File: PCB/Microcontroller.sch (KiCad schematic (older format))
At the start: 19 parts, among them U8 ATSAM4S, Y1 12MHz .25%

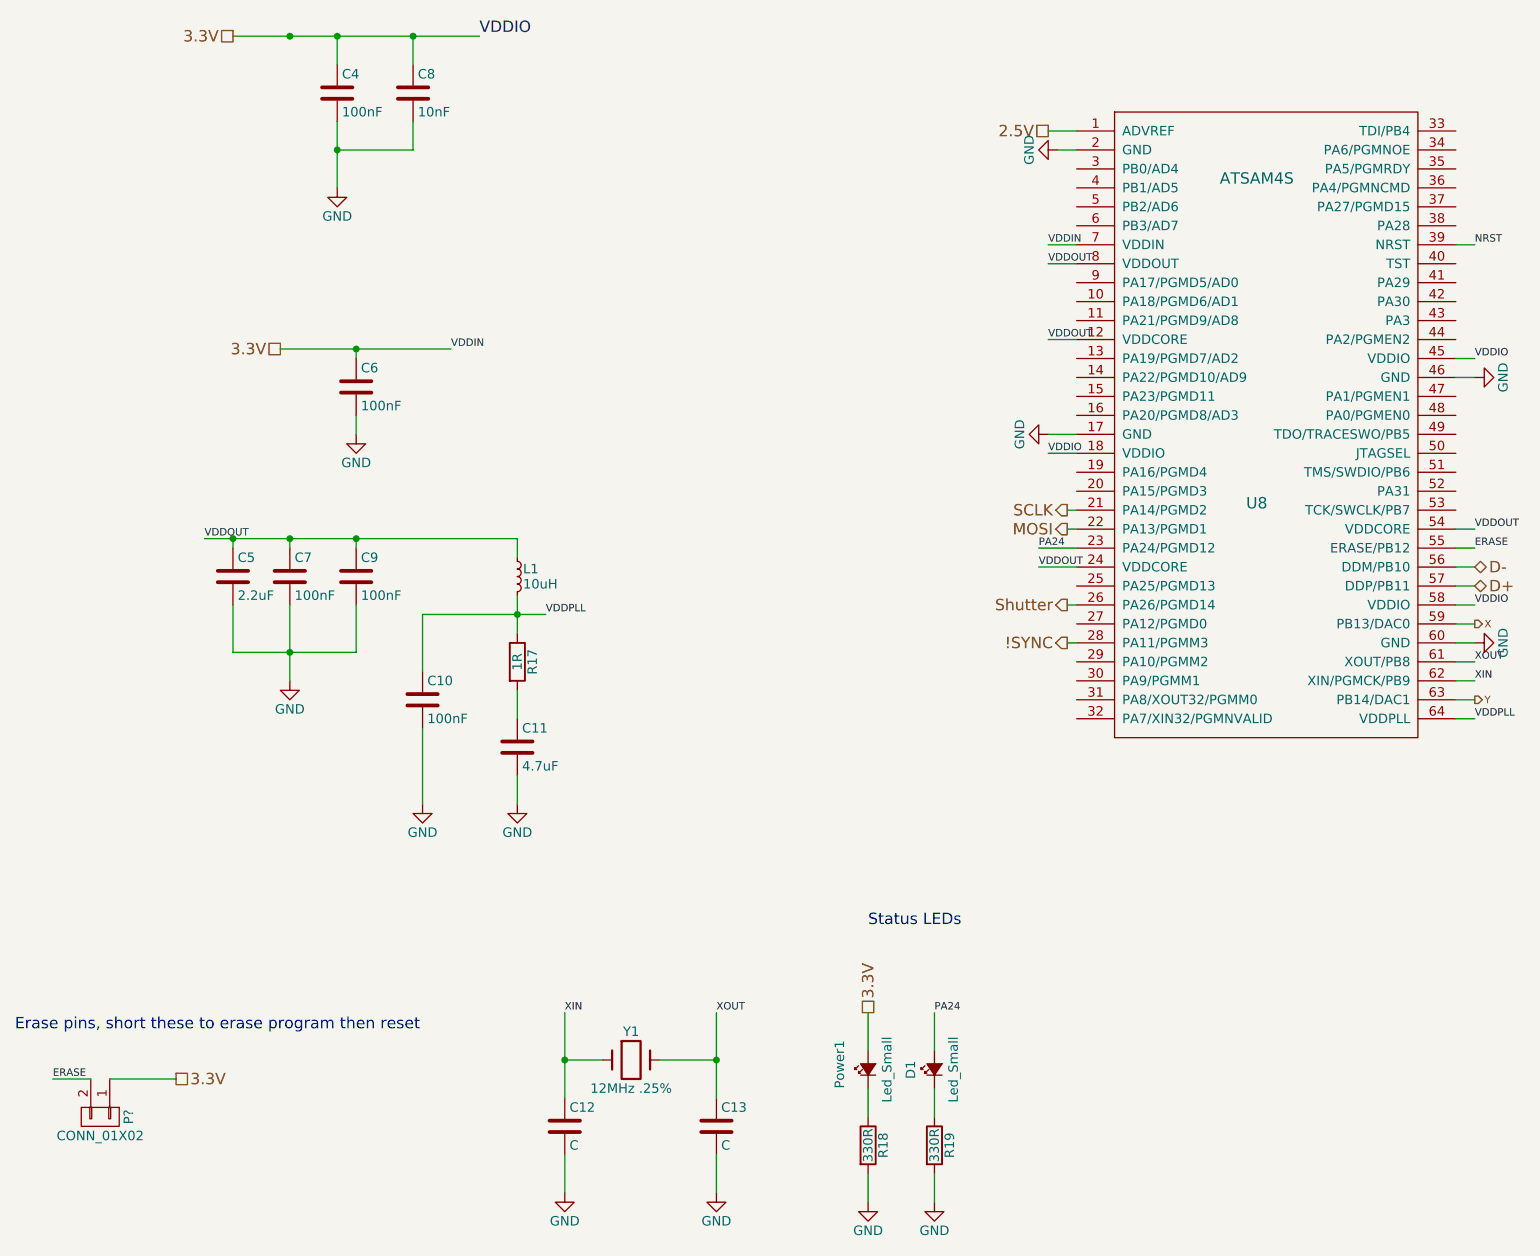
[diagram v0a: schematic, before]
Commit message: Reannotated Components
Annotated components to standards,
TODO: Add Silkscreen for signals on bottom
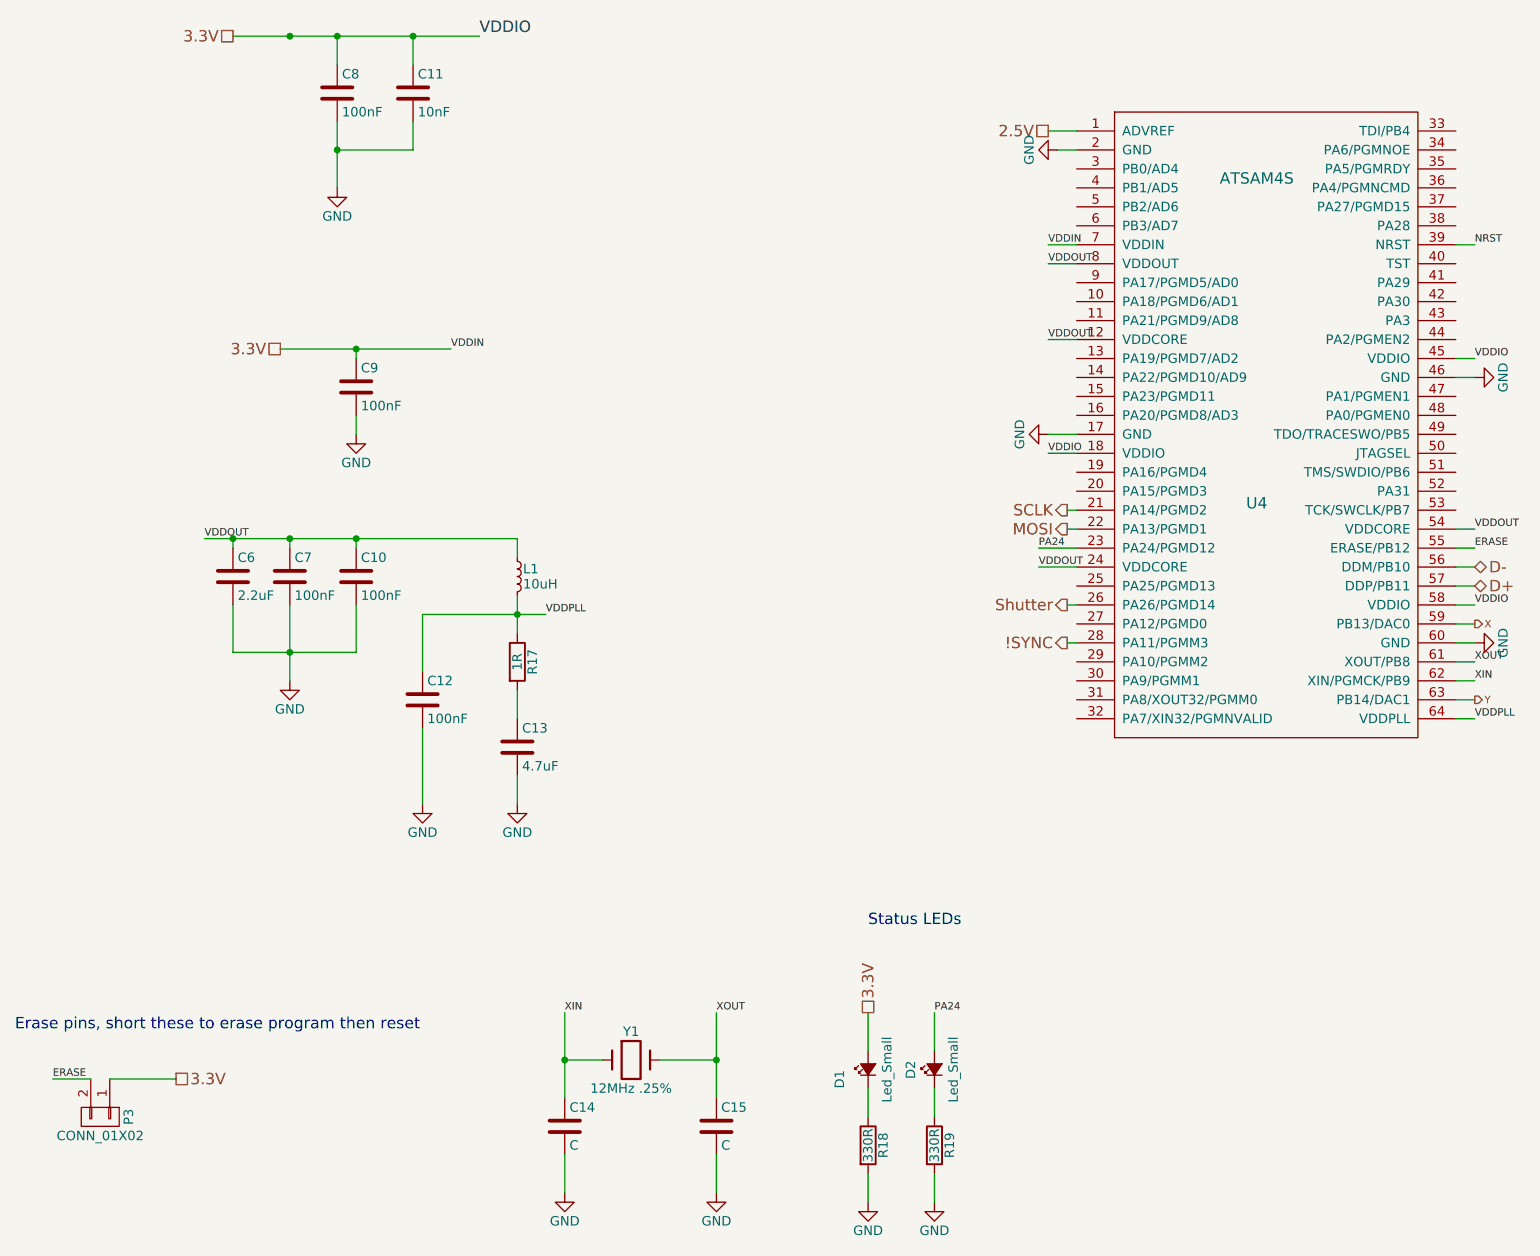
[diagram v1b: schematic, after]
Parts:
- gave numbers to parts that had none: 1
- renumbered C9 to C10, C8 to C11, C10 to C12, C11 to C13, C12 to C14, C13 to C15, C5 to C6, C4 to C8, C6 to C9, Power1 to D1, D1 to D2, U8 to U4
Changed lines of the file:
@@
 $EndDescr
 $Comp
-L ATSAM4S U8
+L ATSAM4S U4
 U 1 1 56B20B8A
 P 7250 2450
-F 0 "U8" H 7250 1137 60  0000 C CNN
+F 0 "U4" H 7250 1137 60  0000 C CNN
 F 1 "ATSAM4S" H 7250 2850 60  0000 C CNN
 F 2 "Housings_QFP:LQFP-64_10x10mm_Pitch0.5mm" H 7250 2850 60  0001 C CNN
@@
 3.3V
 $Comp
-L C C4
+L C C8
 U 1 1 56B26047
 P 2400 1600
-F 0 "C4" H 2425 1700 50  0000 L CNN
+F 0 "C8" H 2425 1700 50  0000 L CNN
 F 1 "100nF" H 2425 1500 50  0000 L CNN
 F 2 "Capacitors_SMD:C_0402" H 2438 1450 50  0001 C CNN
@@
 $EndComp
 $Comp
-L C C8
+L C C11
 U 1 1 56B26074
 P 2800 1600
-F 0 "C8" H 2825 1700 50  0000 L CNN
+F 0 "C11" H 2825 1700 50  0000 L CNN
 F 1 "10nF" H 2825 1500 50  0000 L CNN
 F 2 "Capacitors_SMD:C_0402" H 2838 1450 50  0001 C CNN
@@
 $EndComp
 $Comp
-L C C6
+L C C9
 U 1 1 56B26180
 P 2500 3150
-F 0 "C6" H 2525 3250 50  0000 L CNN
+F 0 "C9" H 2525 3250 50  0000 L CNN
 F 1 "100nF" H 2525 3050 50  0000 L CNN
 F 2 "Capacitors_SMD:C_0402" H 2538 3000 50  0001 C CNN
@@
 $EndComp
 $Comp
-L C C9
+L C C10
 U 1 1 56B262EF
 P 2500 4150
-F 0 "C9" H 2525 4250 50  0000 L CNN
+F 0 "C10" H 2525 4250 50  0000 L CNN
 F 1 "100nF" H 2525 4050 50  0000 L CNN
 F 2 "Capacitors_SMD:C_0402" H 2538 4000 50  0001 C CNN
@@
 $EndComp
 $Comp
-L C C5
+L C C6
 U 1 1 56B263C7
 P 1850 4150
-F 0 "C5" H 1875 4250 50  0000 L CNN
+F 0 "C6" H 1875 4250 50  0000 L CNN
 F 1 "2.2uF" H 1875 4050 50  0000 L CNN
 F 2 "Capacitors_SMD:C_0603" H 1888 4000 50  0001 C CNN
@@
 $EndComp
 $Comp
-L C C10
+L C C12
 U 1 1 56B26699
 P 2850 4800
-F 0 "C10" H 2875 4900 50  0000 L CNN
+F 0 "C12" H 2875 4900 50  0000 L CNN
 F 1 "100nF" H 2875 4700 50  0000 L CNN
 F 2 "Capacitors_SMD:C_0402" H 2888 4650 50  0001 C CNN
@@
 $EndComp
 $Comp
-L C C11
+L C C13
 U 1 1 56B26716
 P 3350 5050
-F 0 "C11" H 3375 5150 50  0000 L CNN
+F 0 "C13" H 3375 5150 50  0000 L CNN
 F 1 "4.7uF" H 3375 4950 50  0000 L CNN
 F 2 "Capacitors_SMD:C_0603" H 3388 4900 50  0001 C CNN
@@
 $EndComp
 $Comp
-L C C12
+L C C14
 U 1 1 56B28036
 P 3600 7050
-F 0 "C12" H 3625 7150 50  0000 L CNN
+F 0 "C14" H 3625 7150 50  0000 L CNN
 F 1 "C" H 3625 6950 50  0000 L CNN
 F 2 "Capacitors_SMD:C_0402" H 3638 6900 50  0001 C CNN
@@
 $EndComp
 $Comp
-L C C13
+L C C15
 U 1 1 56B2808A
 P 4400 7050
-F 0 "C13" H 4425 7150 50  0000 L CNN
+F 0 "C15" H 4425 7150 50  0000 L CNN
 F 1 "C" H 4425 6950 50  0000 L CNN
 F 2 "Capacitors_SMD:C_0402" H 4438 6900 50  0001 C CNN
@@
 	1550 6800 1200 6800
 $Comp
-L Led_Small Power1
+L Led_Small D1
 U 1 1 56BC8AF6
 P 5200 6750
-F 0 "Power1" H 5100 6900 50  0000 L CNN
+F 0 "D1" H 5100 6900 50  0000 L CNN
 F 1 "Led_Small" H 5025 6650 50  0000 L CNN
 F 2 "LEDs:LED_0603" V 5200 6750 50  0001 C CNN
@@
 $EndComp
 $Comp
-L Led_Small D1
+L Led_Small D2
 U 1 1 56BC8E49
 P 5550 6750
-F 0 "D1" H 5500 6875 50  0000 L CNN
+F 0 "D2" H 5500 6875 50  0000 L CNN
 F 1 "Led_Small" H 5375 6650 50  0000 L CNN
 F 2 "LEDs:LED_0603" V 5550 6750 50  0001 C CNN
@@
 Erase pins, short these to erase program then reset
 $Comp
-L CONN_01X02 P?
+L CONN_01X02 P3
 U 1 1 570CE395
 P 1150 7000
-F 0 "P?" H 1150 7150 50  0000 C CNN
+F 0 "P3" H 1150 7150 50  0000 C CNN
 F 1 "CONN_01X02" V 1250 7000 50  0000 C CNN
 F 2 "" H 1150 7000 50  0000 C CNN

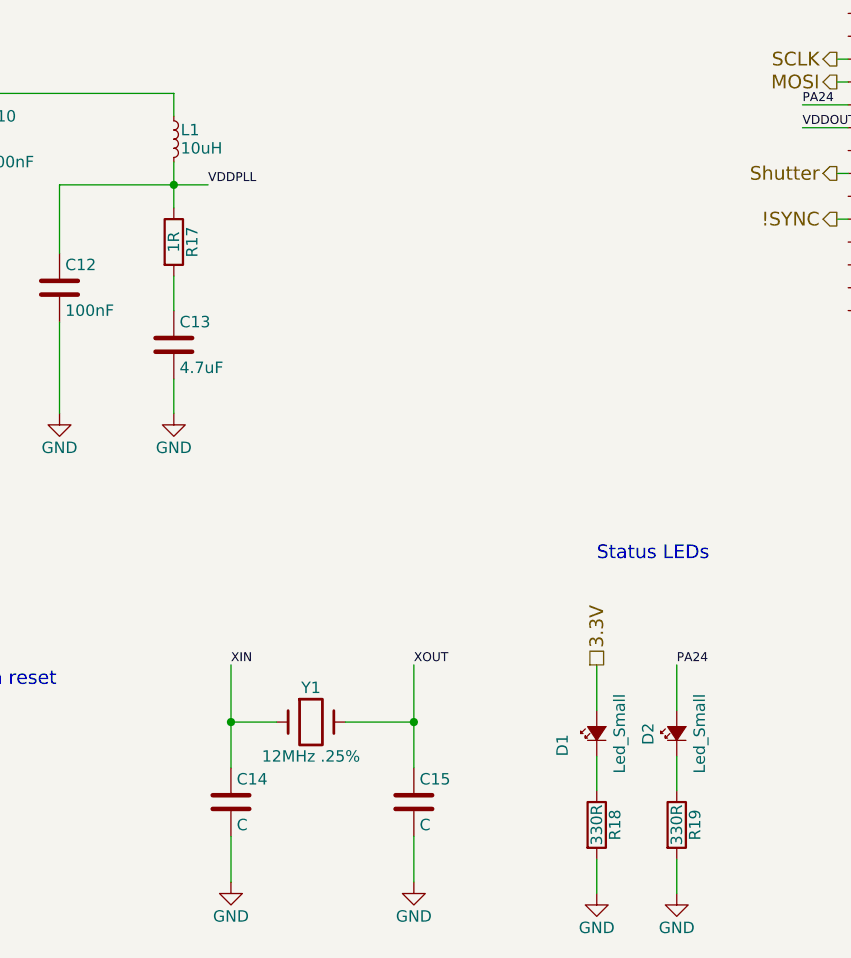
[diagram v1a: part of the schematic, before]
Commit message: Replaced L1 footprint, changed Resistor values
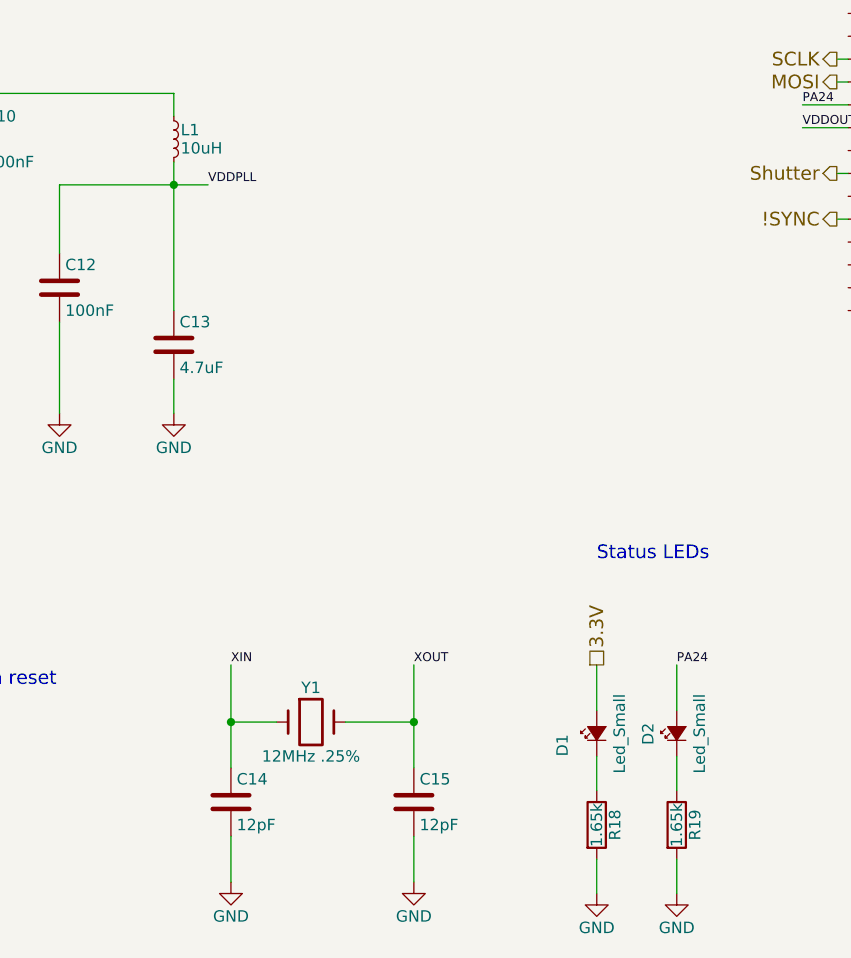
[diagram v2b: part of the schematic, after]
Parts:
- removed R17: 1R, Resistors_SMD:R_0805, symbol R
- C14, C15: value C -> 12pF
- R18, R19: value 330R -> 1.65k
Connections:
- net VDDPLL: now also C13.1
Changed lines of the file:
@@
-$EndComp
-$Comp
-L R R17
-U 1 1 56B26888
-P 3350 4600
-F 0 "R17" V 3430 4600 50  0000 C CNN
-F 1 "1R" V 3350 4600 50  0000 C CNN
-F 2 "Resistors_SMD:R_0805" V 3280 4600 50  0001 C CNN
-F 3 "" H 3350 4600 50  0000 C CNN
-	1    3350 4600
-	1    0    0    -1
 $EndComp
 $Comp
@@
 P 3600 7050
 F 0 "C14" H 3625 7150 50  0000 L CNN
-F 1 "C" H 3625 6950 50  0000 L CNN
+F 1 "12pF" H 3625 6950 50  0000 L CNN
 F 2 "Capacitors_SMD:C_0402" H 3638 6900 50  0001 C CNN
 F 3 "" H 3600 7050 50  0000 C CNN
@@
 P 4400 7050
 F 0 "C15" H 4425 7150 50  0000 L CNN
-F 1 "C" H 4425 6950 50  0000 L CNN
+F 1 "12pF" H 4425 6950 50  0000 L CNN
 F 2 "Capacitors_SMD:C_0402" H 4438 6900 50  0001 C CNN
 F 3 "" H 4400 7050 50  0000 C CNN
@@
 	1700 3950 3350 3950
 Wire Wire Line
-	3350 4250 3350 4450
-Wire Wire Line
-	3350 4750 3350 4900
+	3350 4250 3350 4900
 Wire Wire Line
 	2850 4650 2850 4350
@@
 P 5200 7150
 F 0 "R18" V 5280 7150 50  0000 C CNN
-F 1 "330R" V 5200 7150 50  0000 C CNN
+F 1 "1.65k" V 5200 7150 50  0000 C CNN
 F 2 "Resistors_SMD:R_0805" V 5130 7150 50  0001 C CNN
 F 3 "" H 5200 7150 50  0000 C CNN
@@
 P 5550 7150
 F 0 "R19" V 5630 7150 50  0000 C CNN
-F 1 "330R" V 5550 7150 50  0000 C CNN
+F 1 "1.65k" V 5550 7150 50  0000 C CNN
 F 2 "Resistors_SMD:R_0805" V 5480 7150 50  0001 C CNN
 F 3 "" H 5550 7150 50  0000 C CNN

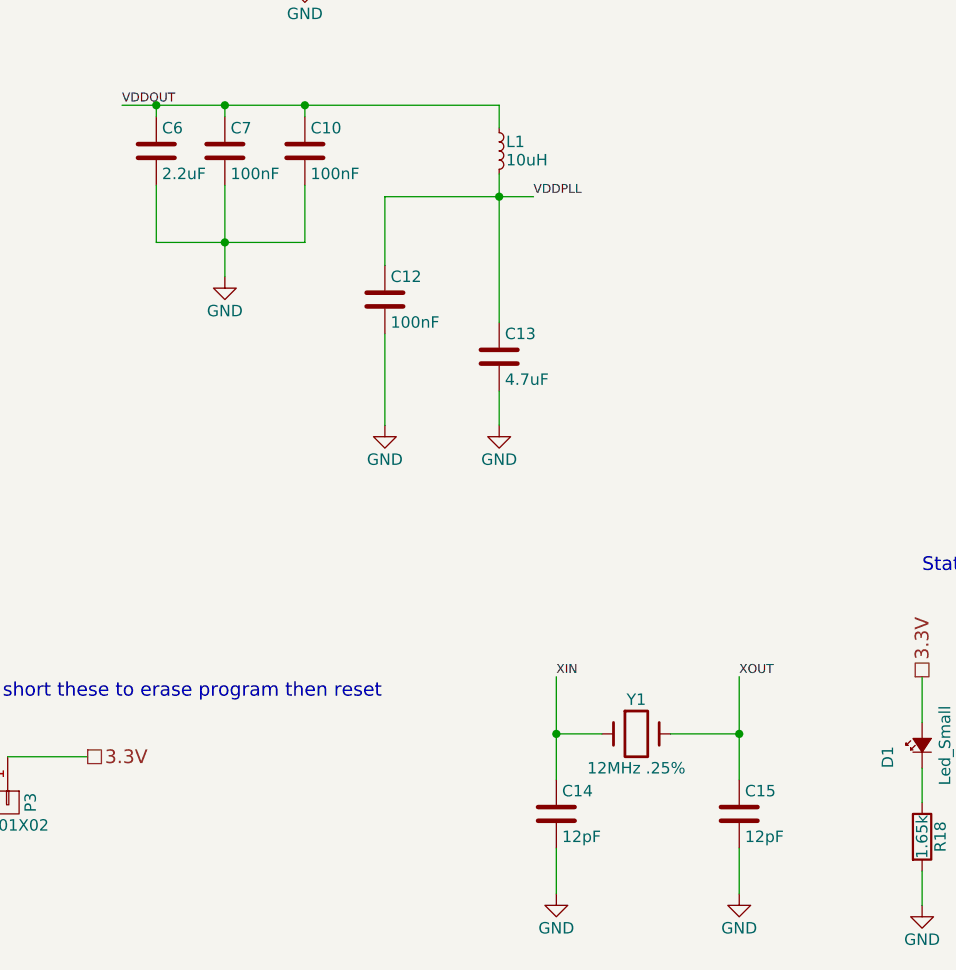
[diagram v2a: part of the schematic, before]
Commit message: Fixed schematic errors, "small" changes to PCB
Flipped DAC, changed component values, removed 1 capacitor, moved c16
from vref to power. Developed an urge to kill kicad
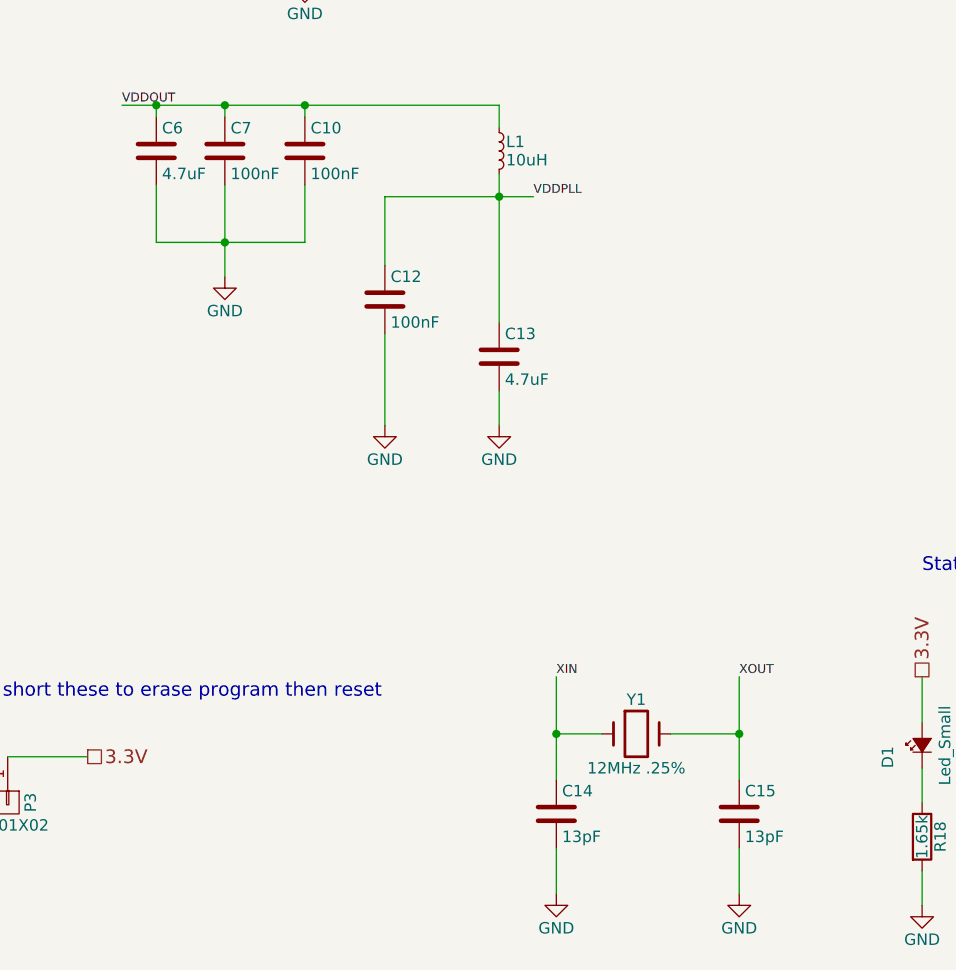
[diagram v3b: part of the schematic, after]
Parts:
- C14, C15: value 12pF -> 13pF
- C6: value 2.2uF -> 4.7uF
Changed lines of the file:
@@
 P 1850 4150
 F 0 "C6" H 1875 4250 50  0000 L CNN
-F 1 "2.2uF" H 1875 4050 50  0000 L CNN
+F 1 "4.7uF" H 1875 4050 50  0000 L CNN
 F 2 "Capacitors_SMD:C_0603" H 1888 4000 50  0001 C CNN
 F 3 "" H 1850 4150 50  0000 C CNN
@@
 P 3600 7050
 F 0 "C14" H 3625 7150 50  0000 L CNN
-F 1 "12pF" H 3625 6950 50  0000 L CNN
+F 1 "13pF" H 3625 6950 50  0000 L CNN
 F 2 "Capacitors_SMD:C_0402" H 3638 6900 50  0001 C CNN
 F 3 "" H 3600 7050 50  0000 C CNN
@@
 P 4400 7050
 F 0 "C15" H 4425 7150 50  0000 L CNN
-F 1 "12pF" H 4425 6950 50  0000 L CNN
+F 1 "13pF" H 4425 6950 50  0000 L CNN
 F 2 "Capacitors_SMD:C_0402" H 4438 6900 50  0001 C CNN
 F 3 "" H 4400 7050 50  0000 C CNN
